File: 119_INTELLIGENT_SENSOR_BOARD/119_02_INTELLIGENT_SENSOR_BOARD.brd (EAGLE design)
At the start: 14.6 x 37.5 mm, 14 parts

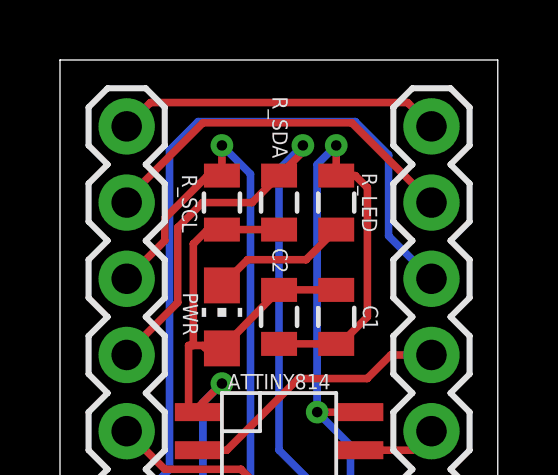
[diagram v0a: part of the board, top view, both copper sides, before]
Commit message: Formed new documentation
Split manual into datasheet, library and notes... added a few more ISC library header defines
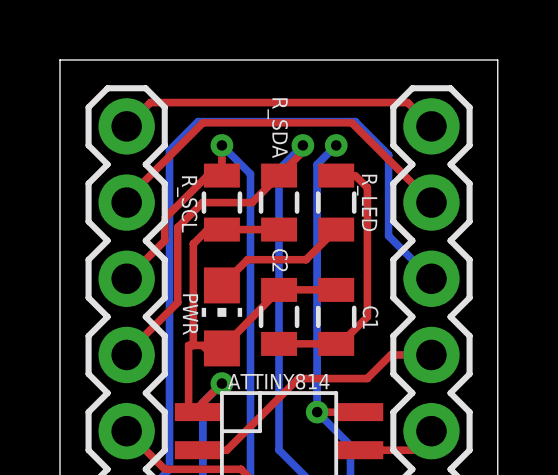
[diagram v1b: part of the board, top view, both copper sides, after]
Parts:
- C1: value (none) -> 0.1u
- C2: value (none) -> 3.3u
- renumbered J1 to PRG, SL1 to V_SEL
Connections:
- removed net N$10: UKMARSBOT.9
- removed net N$11: UKMARSBOT.11
- removed net N$15: UKMARSBOT.10
- removed net N$9: UKMARSBOT.8
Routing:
- net GND: track 56.3 -> 54.6 mm
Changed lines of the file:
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@@
 <attribute name="VALUE" x="7.5946" y="51.816" size="1.27" layer="27" ratio="10" rot="R270"/>
 </element>
-<element name="C1" library="SparkFun-Capacitors" package="0805" value="" x="8.255" y="27.94" smashed="yes" rot="R270">
+<element name="C1" library="SparkFun-Capacitors" package="0805" value="0.1u" x="8.255" y="27.94" smashed="yes" rot="R270">
 <attribute name="NAME" x="9.398" y="27.90825" size="0.508" layer="25" font="vector" ratio="14" rot="SR270" align="center"/>
 <attribute name="VALUE" x="6.858" y="28.956" size="0.4064" layer="27" rot="R270"/>
 </element>
-<element name="C2" library="SparkFun-Capacitors" package="0805" value="" x="6.35" y="27.94" smashed="yes" rot="R270">
+<element name="C2" library="SparkFun-Capacitors" package="0805" value="3.3u" x="6.35" y="27.94" smashed="yes" rot="R270">
 <attribute name="NAME" x="6.38175" y="29.81325" size="0.508" layer="25" font="vector" ratio="14" rot="SR270" align="center"/>
 <attribute name="VALUE" x="4.953" y="28.956" size="0.4064" layer="27" rot="R270"/>
@@
 <attribute name="TP_SIGNAL_NAME" value="" x="3.81" y="12.065" size="1.778" layer="27" display="off"/>
 </element>
-<element name="SL1" library="SparkFun-Connectors" package="1X03" value="" x="8.89" y="3.81" smashed="yes" rot="R180">
+<element name="V_SEL" library="SparkFun-Connectors" package="1X03" value="" x="8.89" y="3.81" smashed="yes" rot="R180">
 <attribute name="VALUE" x="12.446" y="7.6454" size="1.27" layer="27" ratio="10" rot="R180"/>
 </element>
-<element name="J1" library="SparkFun-Connectors" package="1X03" value="" x="8.89" y="7.62" smashed="yes" rot="R180">
+<element name="PRG" library="SparkFun-Connectors" package="1X03" value="" x="8.89" y="7.62" smashed="yes" rot="R180">
 <attribute name="VALUE" x="10.16" y="10.795" size="1.27" layer="27" rot="R180"/>
 </element>
@@
 <contactref element="C1" pad="2"/>
 <contactref element="C2" pad="2"/>
-<contactref element="R_LED" pad="1"/>
 <contactref element="UKMARSBOT" pad="12"/>
 <wire x1="6.35" y1="27.04" x2="8.255" y2="27.04" width="0.254" layer="1"/>
 <contactref element="CONN_GND" pad="TP"/>
 <wire x1="9.29315" y1="32.24685" x2="8.89" y2="32.65" width="0.254" layer="1"/>
-<wire x1="8.255" y1="32.65" x2="8.89" y2="32.65" width="0.254" layer="1"/>
 <wire x1="1.27" y1="6.35" x2="6.35" y2="6.35" width="0.254" layer="1"/>
 <wire x1="6.35" y1="6.35" x2="11.43" y2="6.35" width="0.254" layer="1"/>
@@
 <wire x1="7.62" y1="33.02" x2="7.62" y2="24.765" width="0.254" layer="16"/>
 <wire x1="7.62" y1="24.765" x2="8.73125" y2="23.65375" width="0.254" layer="16"/>
-<wire x1="8.255" y1="32.65" x2="8.255" y2="33.655" width="0.254" layer="1"/>
 <wire x1="8.255" y1="27.04" x2="8.39315" y2="27.04" width="0.254" layer="1"/>
 <wire x1="8.39315" y1="27.04" x2="9.29315" y2="27.94" width="0.254" layer="1"/>
 <wire x1="9.05" y1="24.765" x2="7.62" y2="24.765" width="0.254" layer="1"/>
 <via x="7.62" y="24.765" extent="1-16" drill="0.35"/>
-<contactref element="J1" pad="2"/>
+<contactref element="PRG" pad="2"/>
 <wire x1="6.35" y1="12.065" x2="6.35" y2="7.62" width="0.254" layer="1"/>
 <wire x1="6.35" y1="7.62" x2="6.35" y2="6.35" width="0.254" layer="1"/>
@@
 <wire x1="10.16" y1="8.5504625" x2="8.73125" y2="9.9792125" width="0.254" layer="16"/>
 <wire x1="8.73125" y1="23.65375" x2="8.73125" y2="9.9792125" width="0.254" layer="16"/>
+<contactref element="R_LED" pad="1"/>
+<wire x1="8.89" y1="32.65" x2="8.255" y2="32.65" width="0" layer="19" extent="1-1"/>
+<wire x1="8.255" y1="33.655" x2="8.255" y2="32.65" width="0" layer="19" extent="1-1"/>
 </signal>
 <signal name="5V">
 <contactref element="SENSOR_BOARD" pad="13"/>
 <contactref element="UKMARSBOT" pad="13"/>
-<contactref element="SL1" pad="3"/>
+<contactref element="V_SEL" pad="3"/>
 <wire x1="3.81" y1="3.81" x2="1.27" y2="3.81" width="0.254" layer="16"/>
 <wire x1="3.81" y1="3.81" x2="6.35" y2="1.27" width="0.254" layer="16"/>
@@
 <contactref element="R_SDA" pad="2"/>
 <contactref element="CONN_VDD" pad="TP"/>
-<contactref element="SL1" pad="2"/>
+<contactref element="V_SEL" pad="2"/>
 <wire x1="6.35" y1="28.84" x2="8.255" y2="28.84" width="0.254" layer="1"/>
 <wire x1="6.35" y1="28.84" x2="4.595" y2="27.04" width="0.254" layer="1"/>
@@
 <wire x1="4.445" y1="26.89" x2="3.9075" y2="26.89" width="0.254" layer="1"/>
 <wire x1="3.9075" y1="26.89" x2="3.81" y2="26.9875" width="0.254" layer="1"/>
-<contactref element="J1" pad="3"/>
+<contactref element="PRG" pad="3"/>
 <wire x1="4.445" y1="25.7175" x2="3.81" y2="25.0825" width="0.254" layer="16"/>
 <wire x1="3.81" y1="25.0825" x2="3.81" y2="7.62" width="0.254" layer="16"/>
@@
 <wire x1="6.111875" y1="19.685" x2="6.111875" y2="21.828125" width="0.254" layer="1"/>
 <wire x1="9.05" y1="19.685" x2="6.111875" y2="19.685" width="0.254" layer="1"/>
-<contactref element="J1" pad="1"/>
+<contactref element="PRG" pad="1"/>
 <wire x1="8.89" y1="12.065" x2="8.89" y2="7.62" width="0.254" layer="1"/>
 <wire x1="8.89" y1="7.62" x2="6.35" y2="10.16" width="0.254" layer="16"/>
@@
 <wire x1="7.25" y1="29.845" x2="5.3" y2="29.845" width="0.254" layer="1"/>
 </signal>
-<signal name="N$9">
-<contactref element="UKMARSBOT" pad="8"/>
-</signal>
-<signal name="N$10">
-<contactref element="UKMARSBOT" pad="9"/>
-</signal>
-<signal name="N$11">
-<contactref element="UKMARSBOT" pad="11"/>
-</signal>
-<signal name="N$15">
-<contactref element="UKMARSBOT" pad="10"/>
-</signal>
 <signal name="INTERRUPT">
 <contactref element="U$1" pad="P$4"/>
@@
 </signal>
 <signal name="3V3">
-<contactref element="SL1" pad="1"/>
+<contactref element="V_SEL" pad="1"/>
 <contactref element="UKMARSBOT" pad="14"/>
 <contactref element="SENSOR_BOARD" pad="14"/>
